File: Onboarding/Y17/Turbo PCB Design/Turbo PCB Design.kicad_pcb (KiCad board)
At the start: 2 copper layers, 7 parts

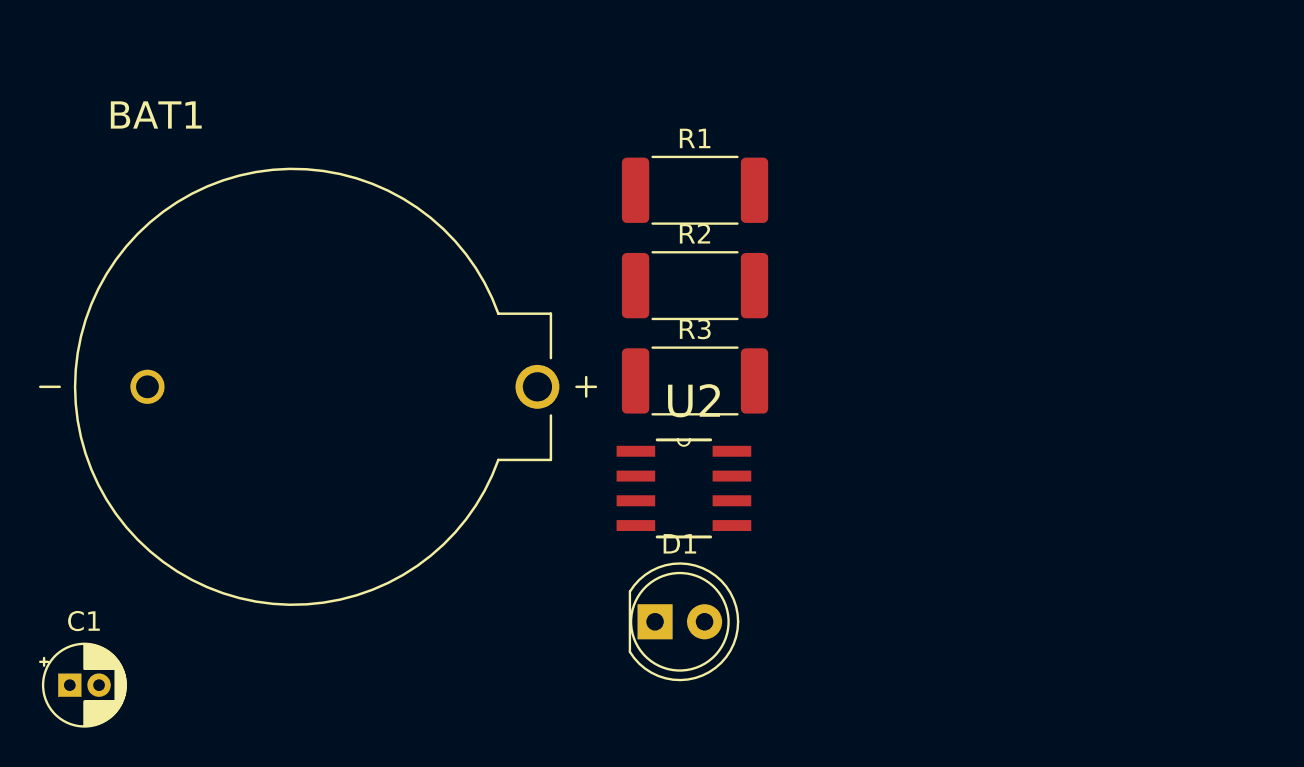
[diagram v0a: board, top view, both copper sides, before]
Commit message: added 1mm through-hole pad to PiE footprint library for onboarding. Finished onboarding footprint.
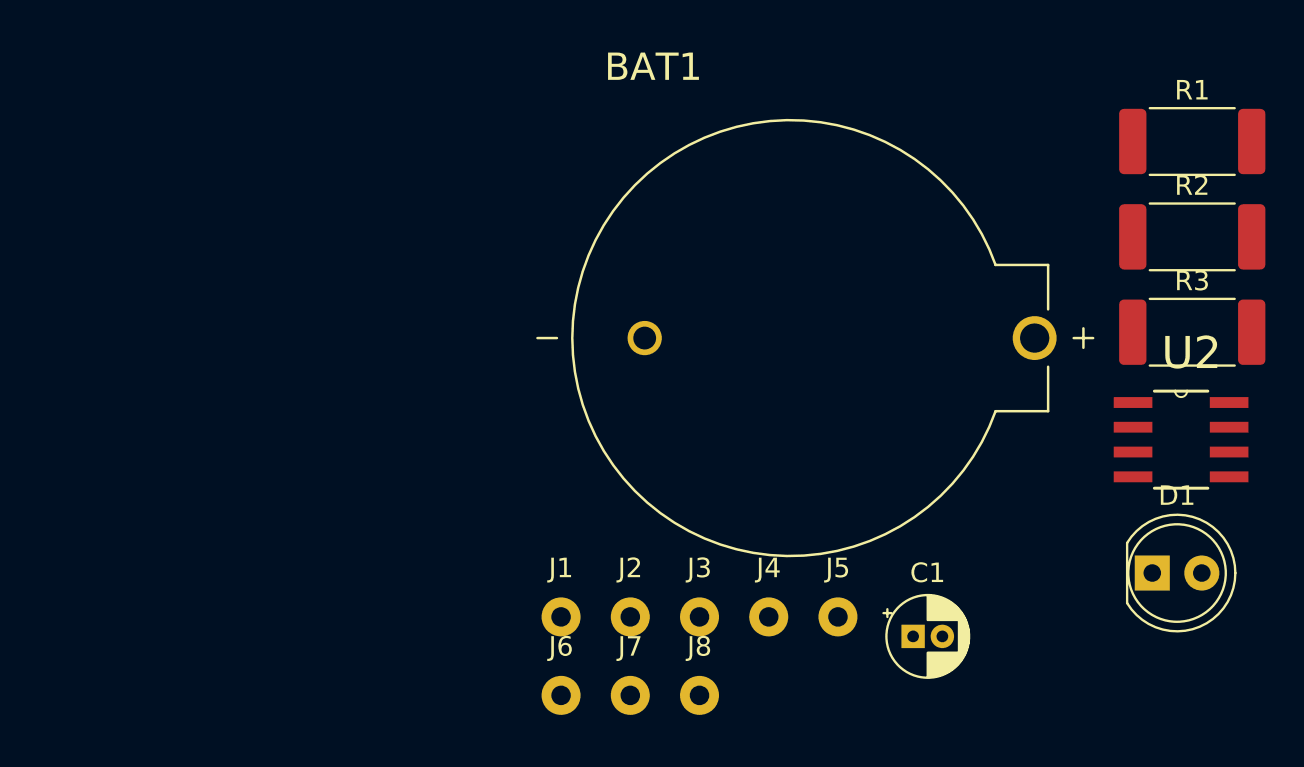
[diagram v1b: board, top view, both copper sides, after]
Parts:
- added J1: Conn_01x01_Socket, PiE_Footprints:MountingHole_1.0mm_M2_Pad, F.Cu at (144.6, 120.2)
- added J2: Conn_01x01_Socket, PiE_Footprints:MountingHole_1.0mm_M2_Pad, F.Cu at (148.2, 120.2)
- added J3: Conn_01x01_Socket, PiE_Footprints:MountingHole_1.0mm_M2_Pad, F.Cu at (151.7, 120.2)
- added J4: Conn_01x01_Socket, PiE_Footprints:MountingHole_1.0mm_M2_Pad, F.Cu at (155.3, 120.2)
- added J5: Conn_01x01_Socket, PiE_Footprints:MountingHole_1.0mm_M2_Pad, F.Cu at (158.8, 120.2)
- added J6: Conn_01x01_Socket, PiE_Footprints:MountingHole_1.0mm_M2_Pad, F.Cu at (144.6, 124.3)
- added J7: Conn_01x01_Socket, PiE_Footprints:MountingHole_1.0mm_M2_Pad, F.Cu at (148.2, 124.3)
- added J8: Conn_01x01_Socket, PiE_Footprints:MountingHole_1.0mm_M2_Pad, F.Cu at (151.7, 124.3)
- moved C1 43.3 mm to (162.7, 119.8)
- moved BAT1 25.6 mm to (158.9, 104.5)
- moved D1 25.6 mm to (175.0, 116.5)
- moved R1 25.6 mm to (177.0, 94.4)
- moved R2 25.6 mm to (177.0, 99.3)
- moved R3 25.6 mm to (177.0, 104.2)
- moved U2 25.6 mm to (176.4, 109.7)
